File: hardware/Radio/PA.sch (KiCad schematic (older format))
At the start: 34 parts, among them U3 RF5110G

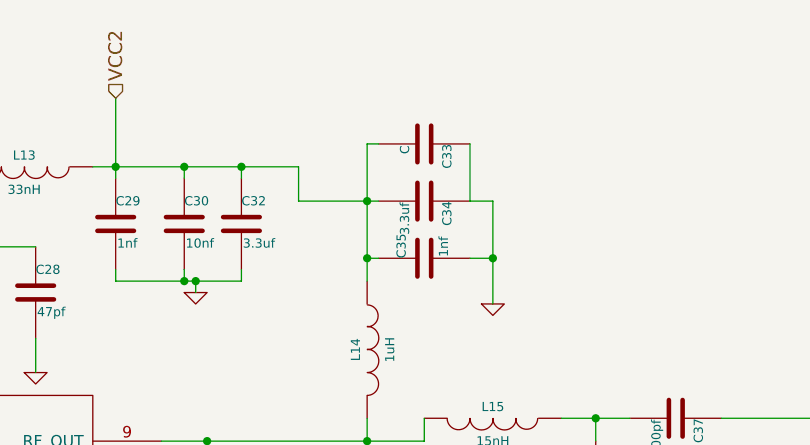
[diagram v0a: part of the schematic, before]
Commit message: Started work on the new power board
Also fixed up some values on the radio board.
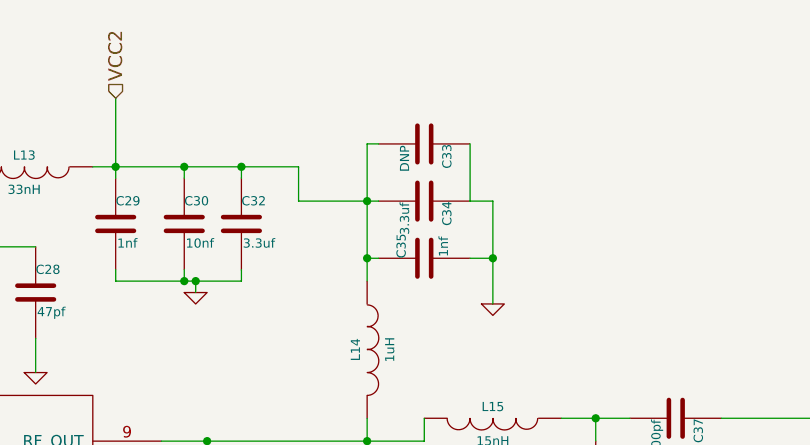
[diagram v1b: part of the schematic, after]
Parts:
- C33: value C -> DNP
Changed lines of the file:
@@
 LIBS:RF5110G
 LIBS:PE42424
-LIBS:dra818Real
 LIBS:RFConn
-LIBS:sma
-LIBS:conn_11x2
-LIBS:SparkFun
-LIBS:smtJmpOpen
-LIBS:neo7
-LIBS:MKL26Z128VLH4
-LIBS:USB
-LIBS:open-project
 LIBS:radio-cache
 EELAYER 25 0
@@
 P 8250 2750
 F 0 "C33" H 8250 2850 40  0000 L CNN
-F 1 "C" H 8256 2665 40  0000 L CNN
+F 1 "DNP" H 8256 2665 40  0000 L CNN
 F 2 "Capacitors_SMD:C_0402" H 8288 2600 30  0001 C CNN
 F 3 "" H 8250 2750 60  0000 C CNN

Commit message: Annotated the schematic and board
Made the numbers increase by 100, so I can just copy this in.
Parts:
- C108: renamed from C14; symbol C -> C-RESCUE-radio
- C109: renamed from C15; symbol C -> C-RESCUE-radio
- C114: renamed from C16; symbol C -> C-RESCUE-radio
- C116: renamed from C29; symbol C -> C-RESCUE-radio
- C118: renamed from C17; symbol C -> C-RESCUE-radio
- C119: renamed from C30; symbol C -> C-RESCUE-radio
- C120: renamed from C18; symbol C -> C-RESCUE-radio
- C121: renamed from C32; symbol C -> C-RESCUE-radio
- C122: renamed from C21; symbol C -> C-RESCUE-radio
- C123: renamed from C27; symbol C -> C-RESCUE-radio
- C124: renamed from C23; symbol C -> C-RESCUE-radio
- C125: renamed from C37; symbol C -> C-RESCUE-radio
- C126: renamed from C26; symbol C -> C-RESCUE-radio
- C128: renamed from C36; symbol C -> C-RESCUE-radio
- C129: renamed from C24; symbol C -> C-RESCUE-radio
- C130: renamed from C22; symbol C -> C-RESCUE-radio
- C131: renamed from C35; symbol C -> C-RESCUE-radio
- C132: renamed from C19; symbol C -> C-RESCUE-radio
- C133: renamed from C20; symbol C -> C-RESCUE-radio
- C134: renamed from C33; symbol C -> C-RESCUE-radio
- C135: renamed from C25; symbol C -> C-RESCUE-radio
- C136: renamed from C28; symbol C -> C-RESCUE-radio
- C137: renamed from C31; symbol C -> C-RESCUE-radio
- C138: renamed from C34; symbol C -> C-RESCUE-radio
- R101: renamed from R1; symbol R -> R-RESCUE-radio
- renumbered L8 to L102, L9 to L105, L10 to L109, L11 to L112, L13 to L113, L15 to L114, L12 to L115, L14 to L116, U3 to U103
